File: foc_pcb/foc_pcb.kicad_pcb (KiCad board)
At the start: 4 copper layers, 48.5 x 48.3 mm, 38 parts, among them IC1 AS5600-ASOT, J1 IMU, J2 BATT_IN, J3 Conn_01x03, J4 power_supply, J5 ESP, U1 DRV8313PWPR

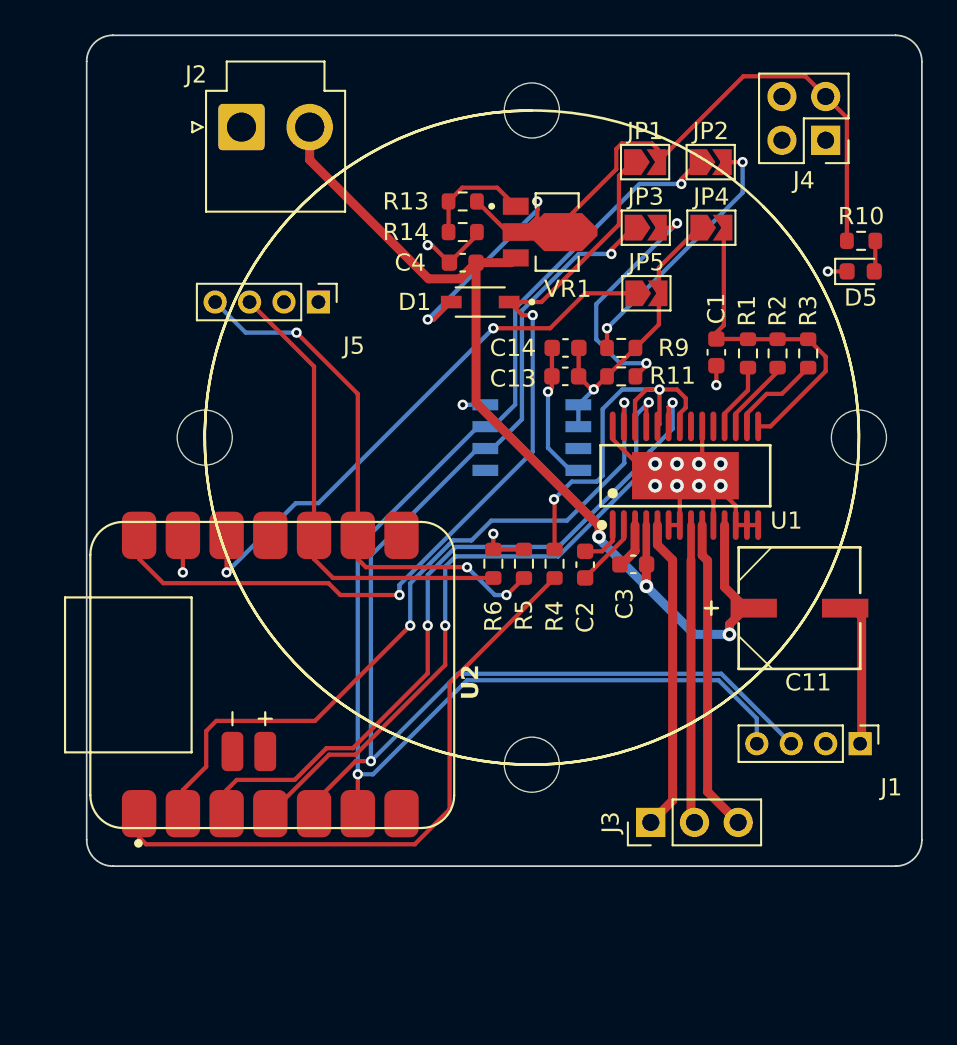
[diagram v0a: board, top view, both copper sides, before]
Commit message: removed rendunant solder jumpers
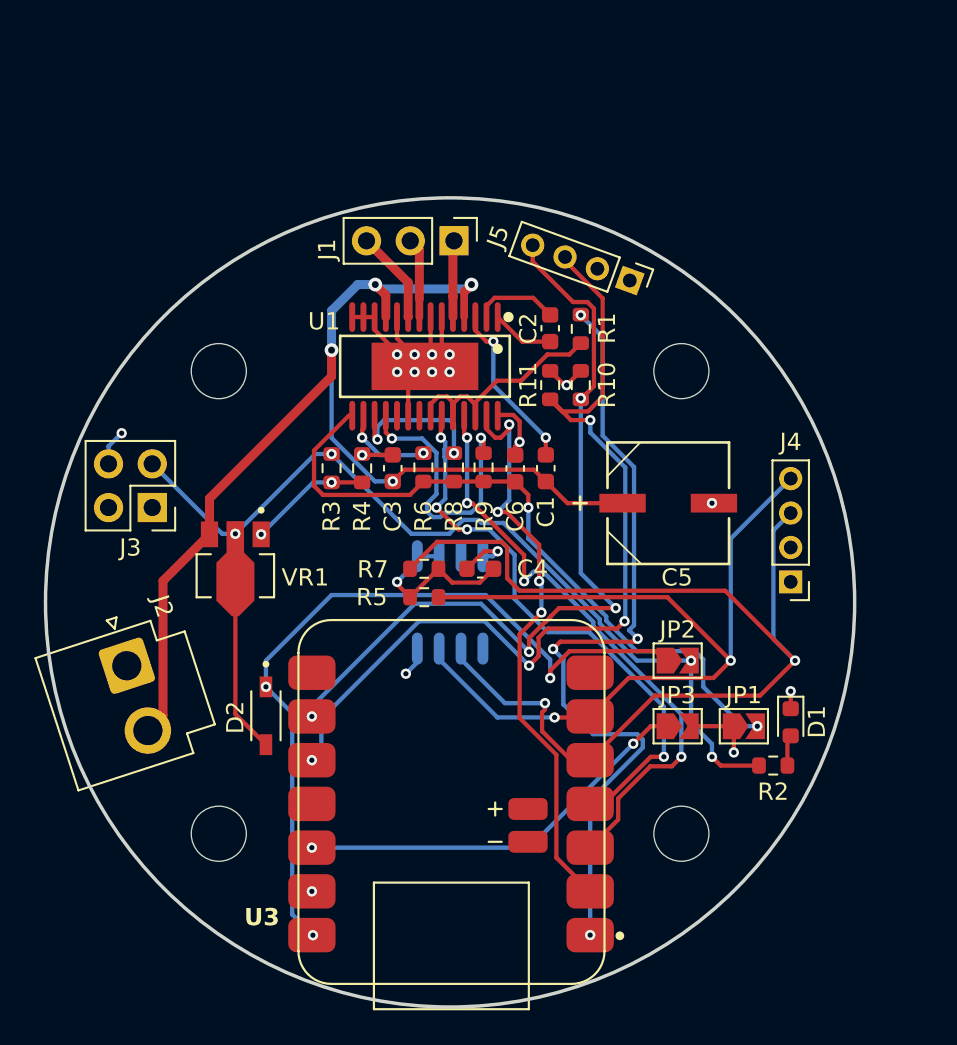
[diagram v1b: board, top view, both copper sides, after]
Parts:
- removed C14: 1uF, Capacitor_SMD:C_0603_1608Metric
- removed IC1: AS5600-ASOT, AS5600-ASOT:SOIC127P600X175-8N
- removed the JP2 at (327.1, 125.7)
- removed the JP3 at (323.3, 129.5)
- added U2: ~, MT6701CT-STD:SOP-8_L4.9-W3.9-P1.27-LS6.0-BL, B.Cu at (311.9, 151.3)
- moved J3 44.6 mm to (294.6, 145.8)
- moved J1 35.7 mm to (312.2, 130.3), turned to -90 degrees
- moved J2 32.0 mm to (293.2, 155.0), turned to -72 degrees
- moved R2 30.9 mm to (330.7, 160.8)
- moved JP1 29.0 mm to (329.0, 158.5)
- moved JP2 29.0 mm to (325.2, 154.7)
- moved D2 27.1 mm to (301.2, 157.9), turned to -90 degrees
- moved VR1 26.8 mm to (299.5, 149.4), turned to -90 degrees
- moved D1 26.5 mm to (331.7, 158.3), turned to -90 degrees
- moved JP3 25.2 mm to (325.2, 158.5)
- moved H3 23.7 mm to (298.5, 137.9), turned to 45 degrees
- moved R6 23.3 mm to (310.4, 143.5), turned to -90 degrees
- moved H1 23.0 mm to (298.5, 164.7), turned to 45 degrees
- moved R8 19.9 mm to (312.2, 143.5), turned to -90 degrees
- moved R5 18.5 mm to (310.4, 151.0), turned to 0 degrees
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- renumbered C3 to C1, C4 to C3, C13 to C4, C11 to C5, C1 to C6, D5 to D1, D1 to D2, H3 to H2, H2 to H3, J3 to J1, J4 to J3, J1 to J4, JP4 to JP1, JP1 to JP2, JP5 to JP3, R4 to R1, R5 to R10, R6 to R11, R10 to R2, R13 to R3, R14 to R4, R9 to R5, R3 to R6, R11 to R7, R2 to R8, R1 to R9, U2 to U3
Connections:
- C4 pad 1: +3.3V -> GND
- C4 pad 2: GND -> +3.3V
- R5 pad 2: Net-(JP2-B) -> /scl
- R7 pad 2: Net-(JP3-B) -> /sda
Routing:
- net /esp_sda: track 27.3 -> 53.4 mm, vias 0 -> 4
- net /scl: track 75.8 -> 50.8 mm
- net /v3p3: track 19.5 -> 39.9 mm, vias 0 -> 2
- net GND: track 48.1 -> 29.1 mm
- net /esp_scl: track 31.0 -> 47.7 mm, vias 3 -> 4
- net Net-(JP2-B): track 15.2 -> 0.00 mm, vias 2 -> 0
- net Net-(JP3-B): track 14.4 -> 0.00 mm, vias 2 -> 0
- net /out1: track 18.2 -> 4.45 mm
- net /out3: track 18.1 -> 5.43 mm
- net /out2: track 17.4 -> 4.65 mm
- net +5V: track 50.0 -> 62.7 mm, vias 2 -> 4
- net /fault: track 3.98 -> 16.4 mm, vias 0 -> 2
- net /en: track 36.4 -> 47.1 mm, vias 0 -> 4
- net /sda: track 72.1 -> 62.5 mm
- net Net-(JP3-A): track 32.5 -> 23.4 mm
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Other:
- board size 48.5 x 48.3 mm -> 47 x 47 mm

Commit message: v3 incoming
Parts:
- moved C2 227.0 mm to (106.8, 51.4)
- moved C5 227.0 mm to (113.7, 61.6)
- moved JP1 227.0 mm to (118.1, 74.5)
- moved R2 227.0 mm to (119.8, 76.8)
- moved D2 227.0 mm to (90.3, 73.9)
- moved H2 227.0 mm to (114.4, 80.8)
- moved R11 227.0 mm to (106.8, 54.7)
- moved R5 227.0 mm to (99.5, 67.0)
- moved R7 227.0 mm to (99.5, 65.4)
- moved R9 227.0 mm to (103.0, 59.5)
- moved U2 227.0 mm to (101.0, 67.3)
- moved U3 227.0 mm to (110.0, 68.5)
- moved VR1 227.0 mm to (88.5, 65.4)
- moved C3 227.0 mm to (97.7, 59.5)
- moved C4 227.0 mm to (102.8, 65.4)
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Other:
- board text added: "AVANINDER.COM"
- board text added: "GimbalFOC"
- board text added: "v3.0"
